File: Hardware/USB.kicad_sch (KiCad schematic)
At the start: 14 parts, among them J5 ??, U9 CP2102N-A02-GQFN24

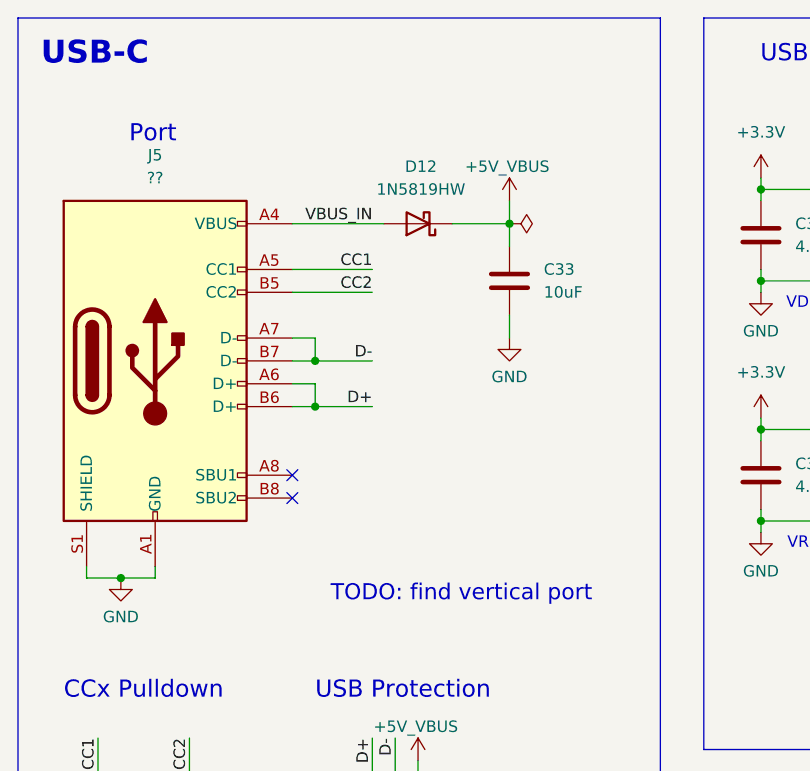
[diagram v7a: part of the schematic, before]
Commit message: added vertical usb c
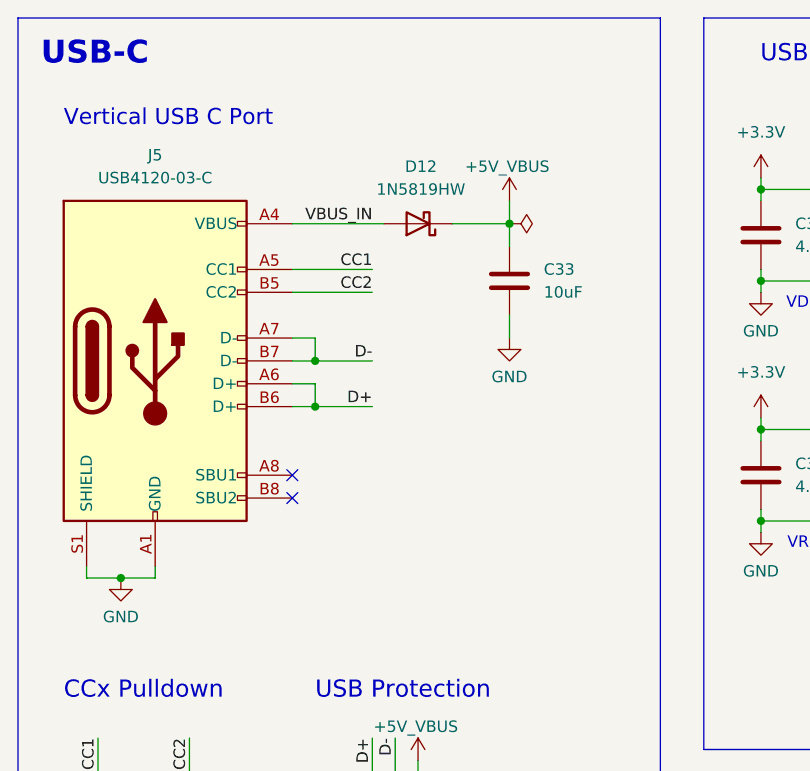
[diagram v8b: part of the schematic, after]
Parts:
- J5: value ?? -> USB4120-03-C; footprint Connector_USB:USB_C_Receptacle_GCT_USB4105-xx-A_16P_TopMnt_Horizontal -> Parts:USB412003C; P/N (none) -> USB4120-03-C
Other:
- note added: "Vertical USB C Port"
- note removed: "Port"
- note removed: "TODO: find vertical port"
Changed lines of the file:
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@@
+		)
+	)
+	(text "Vertical USB C Port"
+		(exclude_from_sim no)
+		(at 20.32 25.4 0)
+		(effects
+			(font
+				(size 1.778 1.778)
+			)
+			(justify left top)
 		)
 	)
@@
 			(font
 				(size 1.27 1.27)
-			)
-		)
-	)
-	(text "Port"
-		(exclude_from_sim no)
-		(at 30.226 28.194 0)
-		(effects
-			(font
-				(size 1.905 1.905)
-				(thickness 0.2381)
 			)
 		)
@@
 			(font
 				(size 1.27 1.27)
-			)
-		)
-	)
-	(text "TODO: find vertical port"
-		(exclude_from_sim no)
-		(at 64.516 79.248 0)
-		(effects
-			(font
-				(size 1.778 1.778)
-				(color 255 30 62 1)
 			)
 		)
@@
 			)
 		)
-		(property "Value" "??"
+		(property "Value" "USB4120-03-C"
 			(at 30.48 33.02 0)
 			(effects
@@
 			)
 		)
-		(property "Footprint" "Connector_USB:USB_C_Receptacle_GCT_USB4105-xx-A_16P_TopMnt_Horizontal"
+		(property "Footprint" "Parts:USB412003C"
 			(at 34.29 53.34 0)
 			(effects
@@
 			)
 		)
-		(property "Datasheet" "https://www.mouser.com/datasheet/2/837/usb4215-3472997.pdf"
+		(property "Datasheet" "https://www.mouser.com/catalog/specsheets/GCT_USB4120.pdf"
 			(at 34.29 53.34 0)
 			(effects
@@
 			)
 		)
-		(property "P/N" ""
+		(property "P/N" "USB4120-03-C"
 			(at 30.48 53.34 0)
 			(effects
